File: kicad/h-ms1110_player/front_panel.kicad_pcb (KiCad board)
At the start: 2 copper layers, 253 x 38.5 mm, 59 parts, among them J1 SSD1322, J10 SWD, J11 USB, J2 POWER, J3 I2C, J4 UART, J5 EXT_INPUT, J6 ENCODER, J7 SYNC, J8 SPI, J9 CONTROL, SW1 OPN, SW10 AUD, SW11 SUB, SW14 RST, SW2 REV, SW4 PLA, SW5 REP, SW7 STP, SW8 FWD, U1 STM32F103CBTx, U3 AMS1117-3.3, U4 AMS1117-3.3, U5 TSOP4538, Y1 8MHz, Y2 32768

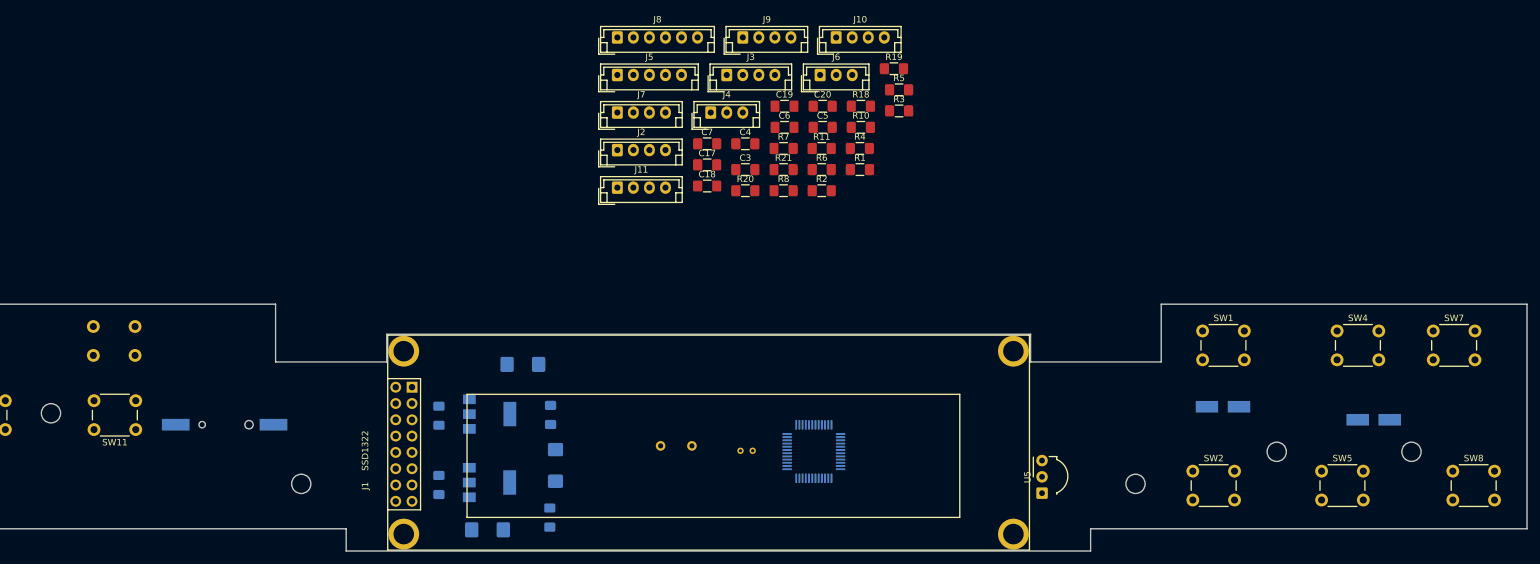
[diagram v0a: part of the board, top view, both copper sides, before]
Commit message: Player board: mcu part
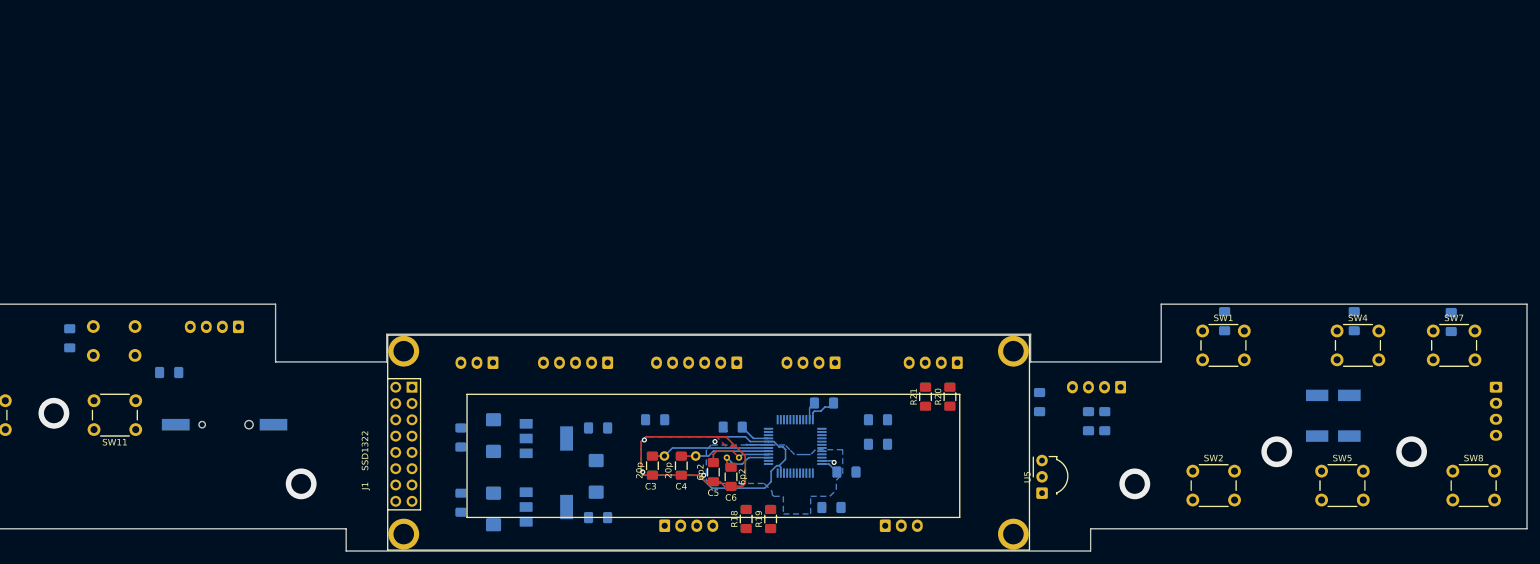
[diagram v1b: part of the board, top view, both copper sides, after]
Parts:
- C17, C18, C19, C20, C7, J10, J11, J2, J3, J4, J5, J6, J7, J8, J9, R1, R10, R11, R2, R3, R4, R5, R6, R7, R8: moved to B.Cu
- moved J10 116.4 mm to (268.0, 104.1), turned to 270 degrees
- moved R4 113.2 mm to (61.2, 101.9)
- moved C7 103.9 mm to (45.7, 96.5), turned to 270 degrees
- moved R3 92.1 mm to (261.0, 94.0), turned to 90 degrees
- moved R2 85.4 mm to (245.9, 93.9), turned to 90 degrees
- moved J11 84.4 mm to (209.5, 104.1), turned to 180 degrees
- moved R19 72.7 mm to (154.9, 124.7), turned to 90 degrees
- moved J3 70.9 mm to (138.4, 125.7)
- moved J4 69.9 mm to (172.8, 125.7)
- moved J6 67.9 mm to (111.7, 100.3), turned to 180 degrees
- moved R18 66.8 mm to (151.1, 124.7), turned to 90 degrees
- moved J7 65.8 mm to (184.0, 100.3), turned to 180 degrees
- moved R7 65.7 mm to (207.0, 109.4), turned to 270 degrees
- moved J2 65.2 mm to (72.0, 94.7), turned to 180 degrees
- moved R5 63.9 mm to (136.9, 109.2)
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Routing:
- net GNDD: track 0.00 -> 108.9 mm, vias 0 -> 5
- net /OSC_OUT: track 0.00 -> 18.6 mm
- net /OSC_IN: track 0.00 -> 13.9 mm
- net /OSC32_OUT: track 0.00 -> 10.7 mm
- net +3V3: track 0.00 -> 9.56 mm
- net /OSC32_IN: track 0.00 -> 9.09 mm
- net +3.3VA: track 0.00 -> 4.81 mm
- net /NRST: track 0.00 -> 3.49 mm
- net (no net): vias 0 -> 5
- added copper zone on B.Cu, net (none)
- added copper zone on F.Cu, net (none)
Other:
- outline, holes or cut-outs redrawn

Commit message: Autorouted player front panel PCB
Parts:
- R5: moved to F.Cu
- moved J3 3.69 mm to (134.7, 125.7)
- moved R18 2.54 mm to (153.7, 124.7)
- moved R19 2.54 mm to (157.5, 124.7)
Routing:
- net GNDD: track 108.9 -> 621.9 mm, vias 5 -> 31
- net +3V3: track 9.56 -> 286.9 mm, vias 0 -> 7
- net +5V: track 0.00 -> 271.8 mm, vias 0 -> 7
- net /KS1: track 0.00 -> 244.5 mm
- net /KS2: track 0.00 -> 240.5 mm
- net /K4: track 0.00 -> 150.4 mm
- net /NRST: track 3.49 -> 152.4 mm, vias 0 -> 2
- net /K3: track 0.00 -> 147.4 mm, vias 0 -> 2
- net /S1: track 0.00 -> 143.4 mm
- net /K2: track 0.00 -> 122.8 mm, vias 0 -> 1
- net /S2: track 0.00 -> 122.2 mm
- net /DISP_CS: track 0.00 -> 115.6 mm, vias 0 -> 3
- net /DISP_DIN: track 0.00 -> 107.0 mm, vias 0 -> 3
- net /DISP_DC: track 0.00 -> 100.6 mm, vias 0 -> 3
- net /K1: track 0.00 -> 100.4 mm, vias 0 -> 1
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- added copper zone on B.Cu, net GNDD
- added copper zone on F.Cu, net GNDD
- removed copper zone on B.Cu, net (none)
- removed copper zone on F.Cu, net (none)

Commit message: Half-routed player PCB
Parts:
- moved J3 20.2 mm to (154.9, 125.7)
- moved R8 14.9 mm to (211.5, 109.6)
- moved C19 10.3 mm to (154.3, 121.4)
- moved R19 10.00 mm to (166.8, 120.9), turned to 270 degrees
- moved R18 9.88 mm to (162.8, 120.9), turned to 270 degrees
- moved D1 7.14 mm to (235.6, 104.1)
- moved D2 7.09 mm to (235.5, 112.4)
- moved R10 5.79 mm to (177.5, 109.2)
- moved R11 5.76 mm to (177.4, 113.3)
- moved BT1 5.59 mm to (70.0, 115.6)
- moved R4 4.98 mm to (62.4, 106.7)
- moved J4 1.19 mm to (174.0, 125.7)
- moved R7 0.67 mm to (207.6, 109.6)
- moved R6 0.67 mm to (203.8, 109.6)
- moved R5 0.64 mm to (136.9, 109.9)
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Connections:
- net Net-(J11-Pad2) renamed /DM
- net Net-(J11-Pad3) renamed /DP
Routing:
- net GNDD: track 621.9 -> 1108.1 mm, vias 31 -> 3
- net /SPI_NSS: track 69.2 -> 22.7 mm, vias 4 -> 3
- net +3V3: track 286.9 -> 244.8 mm, vias 7 -> 5
- net /DISP_DIN: track 107.0 -> 66.0 mm, vias 3 -> 1
- net /NRST: track 152.4 -> 118.5 mm, vias 2 -> 1
- net /SYNC_DATA: track 64.0 -> 32.1 mm, vias 1 -> 0
- net /S1: track 143.4 -> 111.6 mm, vias 0 -> 3
- net /KS1: track 244.5 -> 274.3 mm
- net /DISP_CS: track 115.6 -> 86.4 mm, vias 3 -> 2
- net /K1: track 100.4 -> 124.7 mm, vias 1 -> 2
- net /SYNC_SCK: track 53.0 -> 29.6 mm, vias 3 -> 0
- net /MUTE: track 34.3 -> 13.0 mm, vias 3 -> 0
- net /KS2: track 240.5 -> 259.7 mm, vias 0 -> 1
- net /REMOTE: track 75.9 -> 58.1 mm, vias 2 -> 1
- net /DISP_DC: track 100.6 -> 89.3 mm, vias 3 -> 2
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
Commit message: Finished player board
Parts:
- R8: value 10k -> 1.5k
- moved D2 3.96 mm to (236.0, 108.5)
- moved D1 2.81 mm to (235.9, 101.3)
- moved C7 1.33 mm to (44.4, 96.5)
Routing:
- net /KS2: track 259.7 -> 263.9 mm
- net /K4: track 153.5 -> 156.7 mm
- net /S2: track 114.0 -> 117.1 mm
- net /KS1: track 274.3 -> 271.7 mm
- net /S1: track 111.6 -> 114.1 mm
- net +3V3: track 244.8 -> 246.5 mm
- net GNDD: track 1108.1 -> 1109.5 mm
- net /NRST: track 118.5 -> 119.8 mm
- net /TX: track 25.6 -> 26.5 mm
- net /K3: track 143.3 -> 144.0 mm
- net (no net): vias 0 -> 5
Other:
- board text added: "+3.3VA"
- board text added: "+3V3"
- board text added: "+5V"
- board text added: "AD1"
- board text added: "AD2"
- board text added: "AD3"
- board text added: "BOOT1"
- board text added: "CLK"
- board text added: "CS"
- board text added: "D/C"
- board text added: "D0/CLK"
- board text added: "D1/DIN"
- board text added: "D2"
- board text added: "D3"
- board text added: "D4"
- board text added: "D5"
- board text added: "D6"
- board text added: "D7"
- board text added: "DATA"
- board text added: "DM"
- board text added: "DP"
- board text added: "E/RD"
- board text added: "GND"
- board text added: "IO"
- board text added: "MISO"
- board text added: "MOSI"
- board text added: "MUTE"
- board text added: "NSS"
- board text added: "R/W"
- board text added: "REMOTE"
- board text added: "ROTA"
- board text added: "ROTB"
- board text added: "RST"
- board text added: "RX"
- board text added: "SCK"
- board text added: "SCL"
- board text added: "SDA"
- board text added: "STBY"
- board text added: "TX"
- board text added: "VCC"
